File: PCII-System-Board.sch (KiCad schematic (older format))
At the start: 2 parts

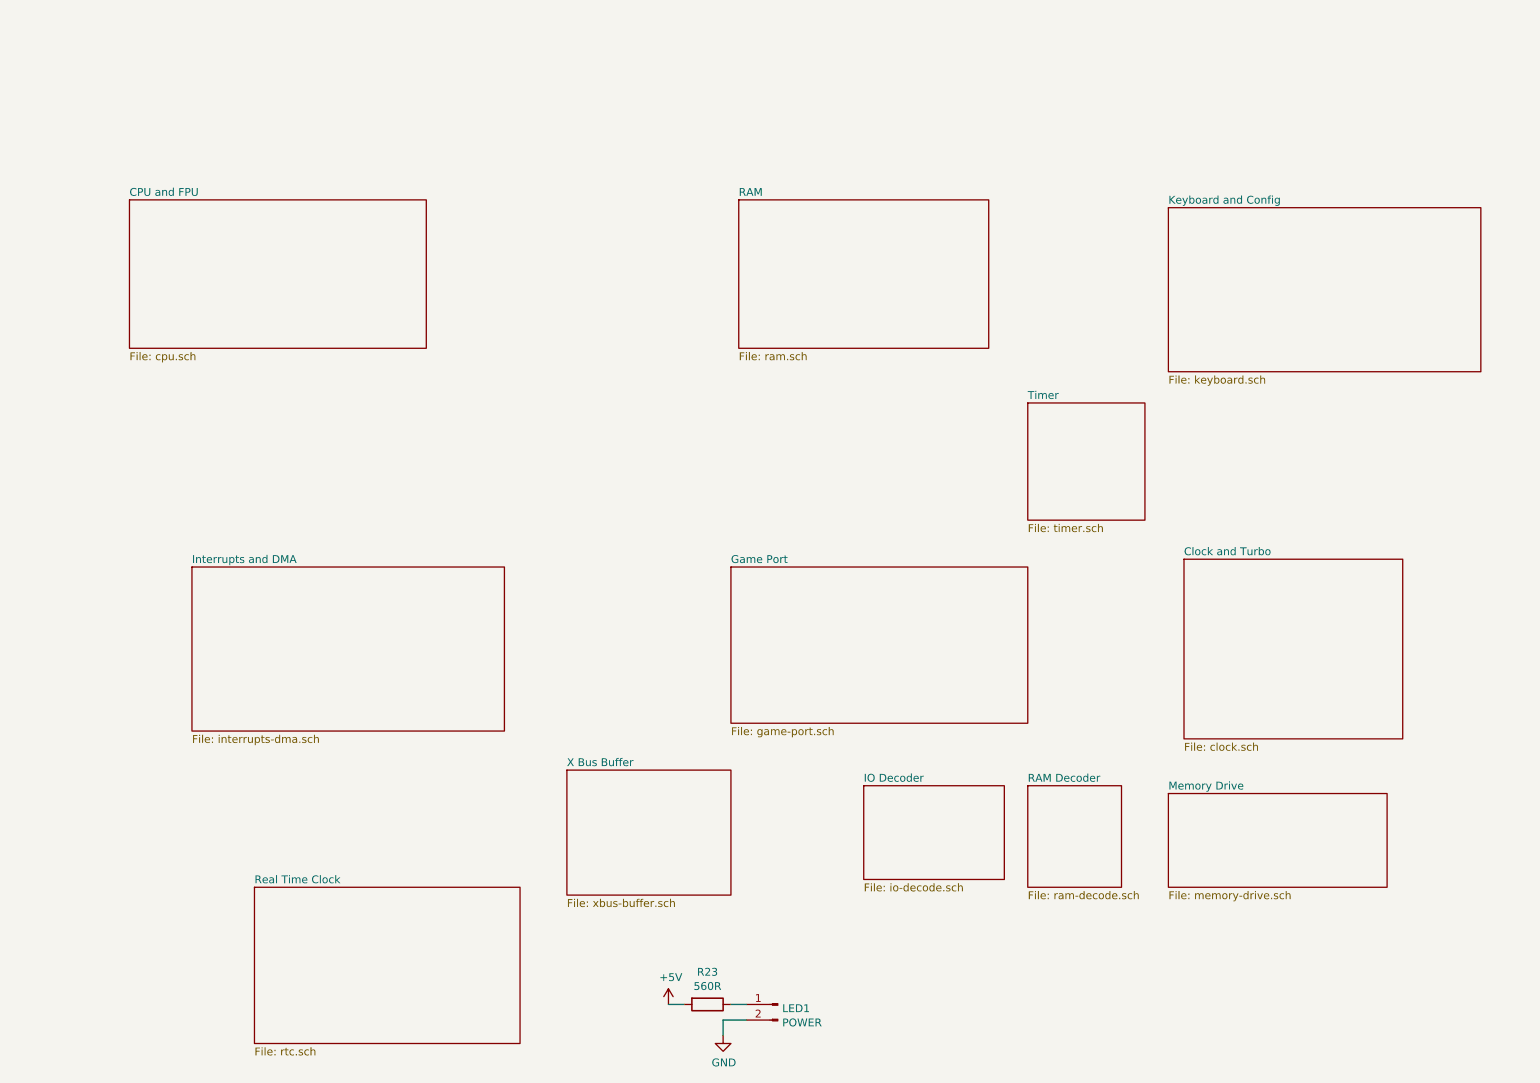
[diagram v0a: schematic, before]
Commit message: Tidy up and map all signals
This fixes up the schematic to:
 - Look presentable
 - Fix all labels connecting sheets
 - Tidy up all loose ends by either inspecting the PCB under
    magnification, measuring with an oscillosope or buzzing
    out with a meter
 - Pass ERC (with 1 exception due to incorrect circuitry around
    pin 33 on the FPU (~RQ~/~GT1~)
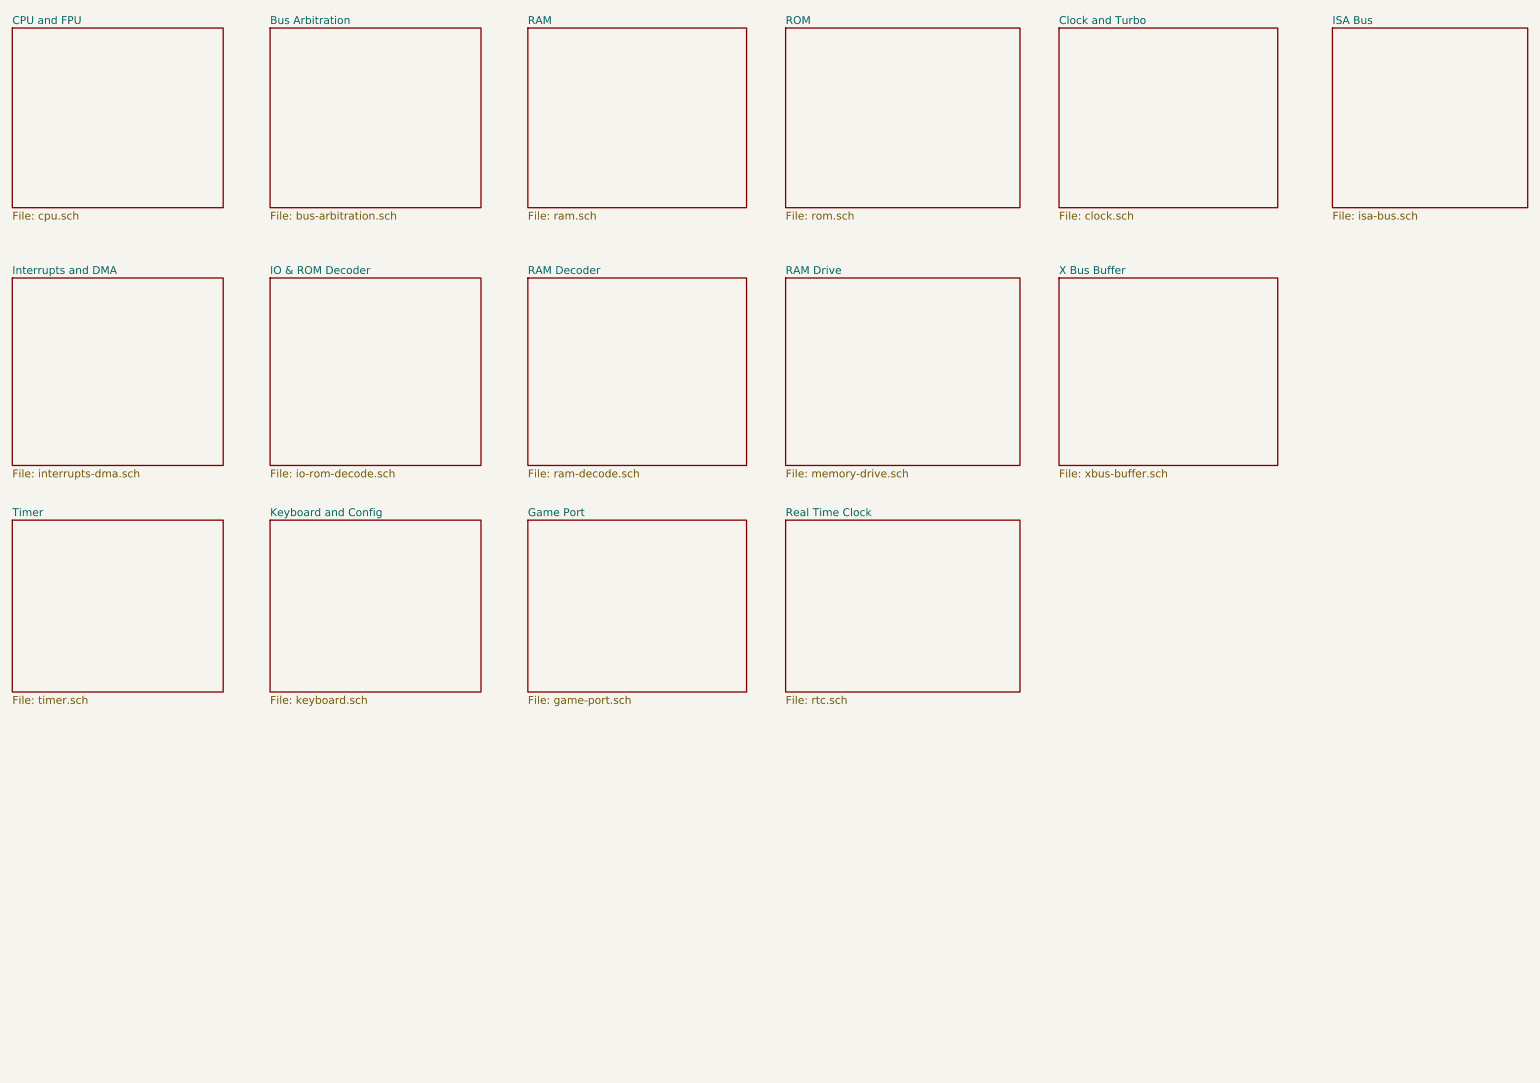
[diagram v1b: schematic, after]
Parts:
- removed LED1: POWER, symbol Connector:Conn_01x02_Male
- removed R23: 560R, symbol Device:R
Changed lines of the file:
@@
 $Descr A4 11693 8268
 encoding utf-8
-Sheet 1 13
-Title ""
+Sheet 1 16
+Title "Wugo PCII System Board"
 Date ""
 Rev ""
@@
 $EndDescr
 $Sheet
-S 1550 1950 1900 950
+S 800  850  1350 1150
 U 5EC54617
 F0 "CPU and FPU" 50
@@
 $EndSheet
 $Sheet
-S 5450 1950 1600 950
+S 4100 850  1400 1150
 U 5EC569A8
 F0 "RAM" 50
@@
 $EndSheet
 $Sheet
-S 5400 4300 1900 1000
+S 4100 4000 1400 1100
 U 5EC569D5
 F0 "Game Port" 50
@@
 $EndSheet
 $Sheet
-S 1950 4300 2000 1050
+S 800  2450 1350 1200
 U 5EC569ED
 F0 "Interrupts and DMA" 50
@@
 $EndSheet
 $Sheet
-S 8200 2000 2000 1050
+S 2450 4000 1350 1100
 U 5EC58627
 F0 "Keyboard and Config" 50
@@
 $EndSheet
 $Sheet
-S 8300 4250 1400 1150
+S 7500 850  1400 1150
 U 5EC5B13F
 F0 "Clock and Turbo" 50
@@
 $EndSheet
 $Sheet
-S 2350 6350 1700 1000
+S 5750 4000 1500 1100
 U 5ECB166B
 F0 "Real Time Clock" 50
@@
 $EndSheet
 $Sheet
-S 4350 5600 1050 800
+S 7500 2450 1400 1200
 U 5F04B123
 F0 "X Bus Buffer" 50
@@
 $EndSheet
 $Sheet
-S 6250 5700 900  600
-U 5F458923
-F0 "IO Decoder" 50
-F1 "io-decode.sch" 50
-$EndSheet
-$Sheet
-S 8200 5750 1400 600
+S 5750 2450 1500 1200
 U 5ECB0F1B
-F0 "Memory Drive" 50
+F0 "RAM Drive" 50
 F1 "memory-drive.sch" 50
 $EndSheet
 $Sheet
-S 7300 5700 600  650
+S 4100 2450 1400 1200
 U 5ED7BC4B
 F0 "RAM Decoder" 50
@@
 $EndSheet
 $Sheet
-S 7300 3250 750  750
+S 800  4000 1350 1100
 U 5F2E6CA0
 F0 "Timer" 50
 F1 "timer.sch" 50
 $EndSheet
-$Comp
-L Connector:Conn_01x02_Male LED1
-U 1 1 5F2F12A0
-P 5700 7100
-F 0 "LED1" H 5672 7074 50  0000 R CNN
-F 1 "POWER" H 5672 6983 50  0000 R CNN
-F 2 "" H 5700 7100 50  0001 C CNN
-F 3 "~" H 5700 7100 50  0001 C CNN
-	1    5700 7100
-	-1   0    0    -1
-$EndComp
-$Comp
-L power:GND #PWR?
-U 1 1 5F2F1A42
-P 5350 7300
-F 0 "#PWR?" H 5350 7050 50  0001 C CNN
-F 1 "GND" H 5355 7127 50  0000 C CNN
-F 2 "" H 5350 7300 50  0001 C CNN
-F 3 "" H 5350 7300 50  0001 C CNN
-	1    5350 7300
-	1    0    0    -1
-$EndComp
-Wire Wire Line
-	5500 7200 5350 7200
-Wire Wire Line
-	5350 7200 5350 7300
-$Comp
-L power:+5V #PWR?
-U 1 1 5F2F1FA2
-P 5000 7100
-F 0 "#PWR?" H 5000 6950 50  0001 C CNN
-F 1 "+5V" H 5015 7273 50  0000 C CNN
-F 2 "" H 5000 7100 50  0001 C CNN
-F 3 "" H 5000 7100 50  0001 C CNN
-	1    5000 7100
-	1    0    0    -1
-$EndComp
-$Comp
-L Device:R R23
-U 1 1 5F2F235E
-P 5250 7100
-F 0 "R23" V 5043 7100 50  0000 C CNN
-F 1 "560R" V 5134 7100 50  0000 C CNN
-F 2 "" V 5180 7100 50  0001 C CNN
-F 3 "~" H 5250 7100 50  0001 C CNN
-	1    5250 7100
-	0    1    1    0
-$EndComp
-Wire Wire Line
-	5500 7100 5400 7100
-Wire Wire Line
-	5100 7100 5000 7100
+$Sheet
+S 2450 850  1350 1150
+U 5EE4AF7F
+F0 "Bus Arbitration" 50
+F1 "bus-arbitration.sch" 50
+$EndSheet
+$Sheet
+S 5750 850  1500 1150
+U 615731E6
+F0 "ROM" 50
+F1 "rom.sch" 50
+$EndSheet
+$Sheet
+S 9250 850  1250 1150
+U 61708DAD
+F0 "ISA Bus" 50
+F1 "isa-bus.sch" 50
+$EndSheet
+$Sheet
+S 2450 2450 1350 1200
+U 5F458923
+F0 "IO & ROM Decoder" 50
+F1 "io-rom-decode.sch" 50
+$EndSheet
 $EndSCHEMATC
